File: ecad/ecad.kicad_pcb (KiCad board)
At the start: 2 copper layers, 99.2 x 85.3 mm, 140 parts, among them J1 Conn_01x22_Pin, J10 USB_C, J11 Conn_01x02_Pin, J2 Conn_01x22_Pin, J3 USB_C, J4 Conn_01x22_Pin, J5 Conn_01x22_Pin, J6 Conn_01x22_Pin, J7 Conn_01x22_Pin, J8 Conn_01x03_Pin, J9 Conn_01x03_Pin, U1 ESP32-CAM, U10 4069, U11 FT232RL, U12 4069, U13 4069, U16 AMS1117-3.3, U17 LM2596S-ADJ, U2 ESP32-WROOM-32, U3 ESP32-WROOM-32, U4 ESP32-S3, U5 4069, U6 4069, U7 4069, U8 4069, U9 4069

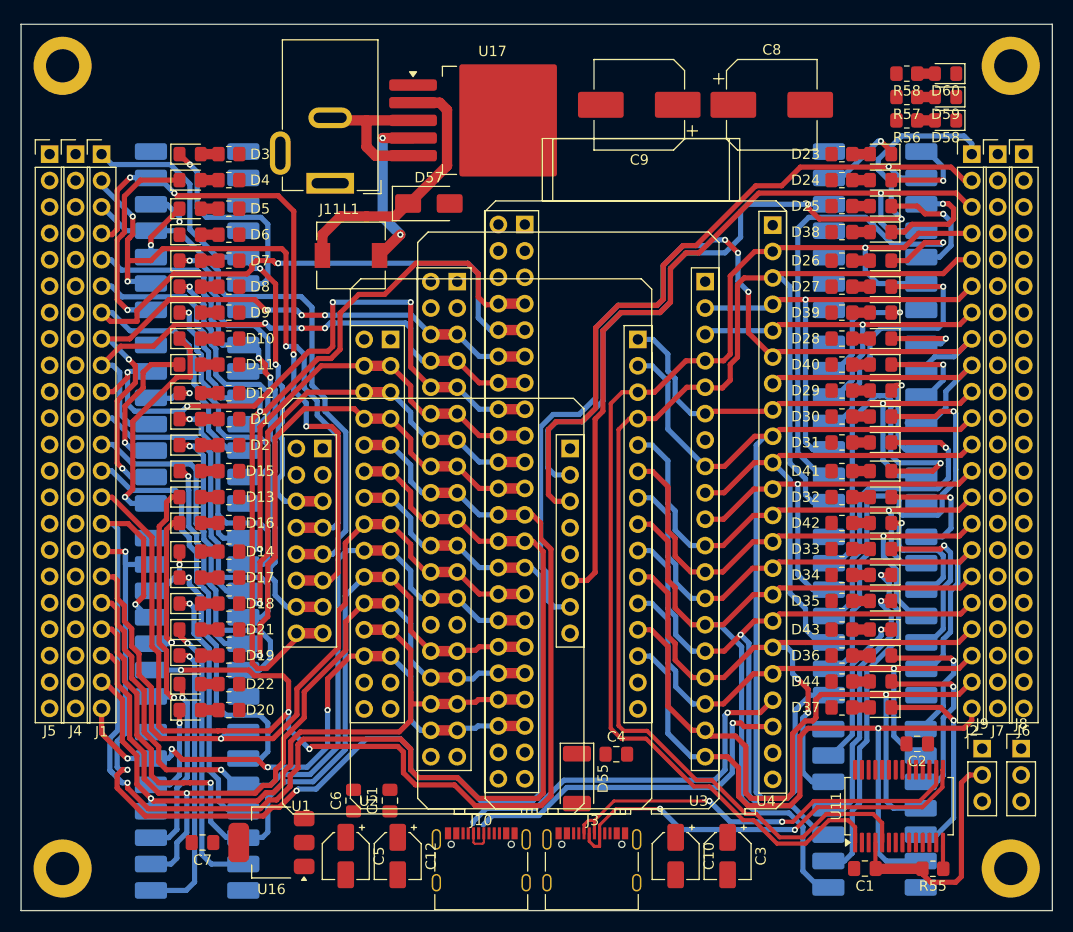
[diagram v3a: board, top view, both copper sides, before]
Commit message: feat (ecad): update PCB design
Connect power
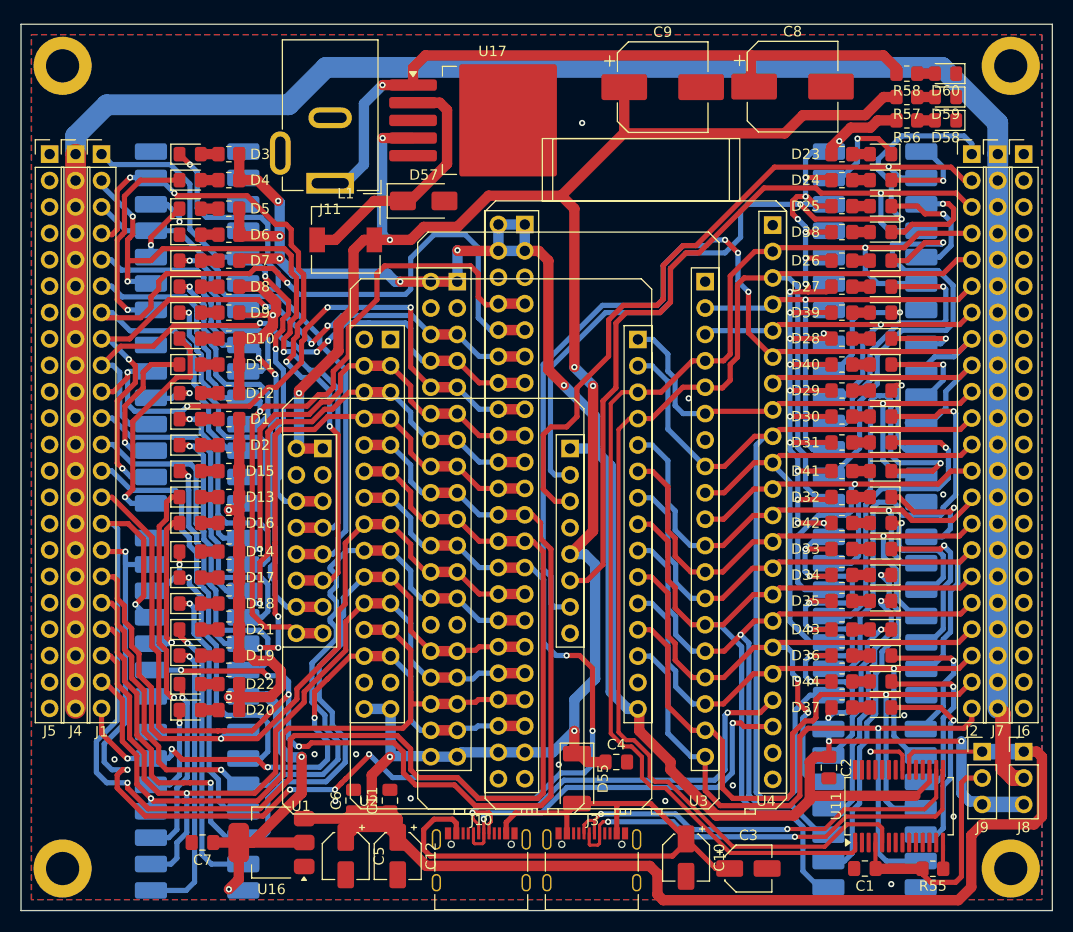
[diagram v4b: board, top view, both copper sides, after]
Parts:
- moved C2 8.80 mm to (129.5, 87.0), turned to -90 degrees
- moved C9 2.82 mm to (113.5, 21.6), turned to 0 degrees
- moved C8 2.66 mm to (126.0, 21.5)
- moved C3 2.33 mm to (121.8, 96.8), turned to 0 degrees
- moved L1 1.58 mm to (83.0, 36.2)
- moved C10 1.01 mm to (115.8, 95.7)
- moved C4 0.75 mm to (109.0, 86.5)
- moved D57 0.56 mm to (90.5, 32.5)
- moved J8 0.38 mm to (148.2, 85.5)
- moved J9 0.29 mm to (144.2, 85.5)
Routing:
- net +3.3V: track 0.00 -> 431.3 mm, vias 0 -> 39
- net +5V: track 15.8 -> 311.1 mm, vias 2 -> 7
- net VCC: track 0.00 -> 213.5 mm
- net +12V: track 0.00 -> 67.7 mm, vias 0 -> 1
- net VBUS: track 0.00 -> 65.1 mm
- net Earth: track 15.5 -> 4.99 mm, vias 0 -> 15
- net S3_GPIO05: track 72.4 -> 79.7 mm
- net GPIO27_X38: track 121.6 -> 127.3 mm, vias 3 -> 7
- net S3_USB+: track 36.9 -> 42.6 mm, vias 1 -> 2
- net GPIO05_X38: track 39.9 -> 44.2 mm
- net GPIO12_X38: track 78.3 -> 82.6 mm
- net CAM_GPIO04: track 94.6 -> 90.9 mm
- net GPIO13_X38: track 83.3 -> 86.4 mm
- net GPIO25_X38: track 134.3 -> 137.4 mm, vias 3 -> 4
- net GPIO26_X38: track 134.9 -> 137.5 mm
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- added copper zone on B.Cu, net Earth
- added copper zone on F.Cu, net Earth

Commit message: chore (ecad): update PCB design
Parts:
- removed C10: 1u, Capacitor_SMD:CP_Elec_4x5.4
- removed C11: 100n, Capacitor_SMD:C_0805_2012Metric_Pad1.18x1.45mm_HandSolder
- removed C12: 4.7u, Capacitor_SMD:CP_Elec_4x5.4
- moved C1 0.75 mm to (133.0, 97.5)
- moved C2 0.75 mm to (129.5, 87.8)
- moved R55 0.75 mm to (139.5, 97.5)
- moved U11 0.75 mm to (136.2, 91.5)
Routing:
- net +3.3V: track 431.3 -> 450.7 mm, vias 39 -> 42
- net +5V: track 311.1 -> 302.2 mm
- net CAM_GPIO12: track 51.2 -> 54.0 mm
- net S3_USB-: track 38.8 -> 41.0 mm
- net Net-(D8-K): track 21.1 -> 23.2 mm
- net CAM_GPIO14: track 67.3 -> 69.2 mm
- net CAM_GPIO13: track 66.0 -> 67.9 mm
- net Net-(D6-K): track 3.72 -> 5.07 mm
- net FLASH_D1: track 51.3 -> 52.4 mm
- net S3_USB+: track 42.6 -> 41.6 mm
- net Net-(D10-K): track 21.8 -> 22.3 mm
- net Vdrive: track 23.0 -> 23.6 mm
- net S3_GPIO05: track 79.7 -> 80.3 mm
- net Earth: track 4.99 -> 5.24 mm, vias 15 -> 16
- net Net-(D16-K): vias 2 -> 1
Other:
- board text added: "12V"
- board text added: "3V3"
- board text added: "5V"
